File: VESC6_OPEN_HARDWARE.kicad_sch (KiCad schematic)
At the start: 20 parts, among them P1 USB_OTG, P2 CAN2, P3 SWD, P4 HALL/Encoder, P5 CAN1, P6 ADC_SWITCH

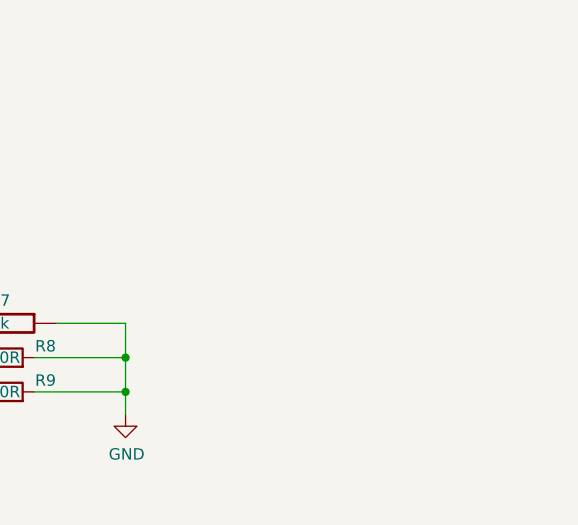
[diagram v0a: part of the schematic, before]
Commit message: mounting holes, more grounding and routing
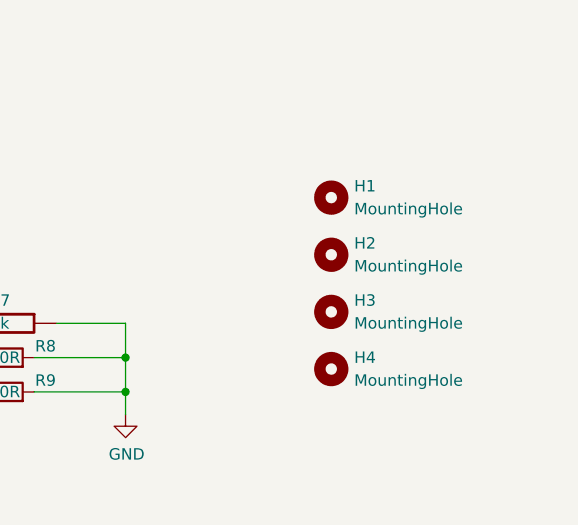
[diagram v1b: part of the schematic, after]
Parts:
- added H1, H2, H3, H4: MountingHole, CustomFootprints:MountingHole_3mm, symbol Mechanical:MountingHole

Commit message: Release
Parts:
- removed D1: BLUE, Diode_SMD:D_0603_1608Metric, symbol Device:LED
- removed R7: 1k, Resistor_SMD:R_0603_1608Metric, symbol BLDC_4-rescue:R-RESCUE-BLDC_4
- D3: value GREEN -> WHITE; LCSC part no. C12624 -> C2290
- P3: LCSC part no. 23390339 -> C160405

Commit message: Release1
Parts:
- D3: Link https://jlcpcb.com/partdetail/EverlightElec-19_217_GHC_YR1S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 -> (none); MFP 19-217/GHC-YR1S2/3T -> (none)
- P1: Link https://jlcpcb.com/partdetail/Korean_HropartsElec-U_D_M5DD_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 -> (none); MFP U-D-M5DD-W-1 -> (none)
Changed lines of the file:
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@@
 			)
 		)
-		(property "Datasheet" "https://www.molex.com/content/dam/molex/molex-dot-com/products/automated/en-us/salesdrawingpdf/505/505567/5055670471_sd.pdf?inline"
+		(property "Datasheet" ""
 			(at 53.34 59.69 0)
 			(effects
@@
 			)
 		)
-		(property "Datasheet" "https://datasheet.lcsc.com/lcsc/1811101510_Everlight-Elec-19-217-GHC-YR1S2-3T_C72043.pdf"
+		(property "Datasheet" ""
 			(at 165.1 153.67 0)
 			(effects
@@
 			)
 		)
-		(property "Link" "https://jlcpcb.com/partdetail/EverlightElec-19_217_GHC_YR1S23T/C72043"
+		(property "Link" ""
 			(at 165.1 153.67 0)
 			(effects
@@
 			)
 		)
-		(property "MFP" "19-217/GHC-YR1S2/3T"
+		(property "MFP" ""
 			(at 165.1 153.67 0)
 			(effects
@@
 			)
 		)
-		(property "Datasheet" "https://www.molex.com/content/dam/molex/molex-dot-com/products/automated/en-us/salesdrawingpdf/482/48258/482580001_sd.pdf?"
+		(property "Datasheet" ""
 			(at 58.42 38.1 0)
 			(effects
@@
 			)
 		)
-		(property "Link" "https://jlcpcb.com/partdetail/Korean_HropartsElec-U_D_M5DD_W1/C145795"
+		(property "Link" ""
 			(at 54.61 36.83 0)
 			(effects
@@
 			)
 		)
-		(property "MFP" "U-D-M5DD-W-1"
+		(property "MFP" ""
 			(at 54.61 36.83 0)
 			(effects
@@
 			)
 		)
-		(property "Datasheet" "~"
+		(property "Datasheet" ""
 			(at 74.93 31.75 0)
 			(effects
@@
 			)
 		)
-		(property "Datasheet" "https://www.molex.com/content/dam/molex/molex-dot-com/products/automated/en-us/salesdrawingpdf/505/505567/5055670471_sd.pdf?inline"
+		(property "Datasheet" ""
 			(at 41.91 59.69 0)
 			(effects
@@
 			)
 		)
-		(property "Datasheet" "~"
+		(property "Datasheet" ""
 			(at 217.17 132.08 0)
 			(effects
@@
 			)
 		)
-		(property "Datasheet" "https://www.molex.com/content/dam/molex/molex-dot-com/products/automated/en-us/salesdrawingpdf/505/505567/5055670671_sd.pdf?inline"
+		(property "Datasheet" ""
 			(at 52.07 91.44 0)
 			(effects
@@
 			)
 		)
-		(property "Datasheet" "https://www.molex.com/content/dam/molex/molex-dot-com/products/automated/en-us/salesdrawingpdf/505/505567/5055670471_sd.pdf?inline"
+		(property "Datasheet" ""
 			(at 102.87 20.32 0)
 			(effects
@@
 			)
 		)
-		(property "Datasheet" "~"
+		(property "Datasheet" ""
 			(at 217.17 138.43 0)
 			(effects
@@
 			)
 		)
-		(property "Datasheet" "https://www.molex.com/content/dam/molex/molex-dot-com/products/automated/en-us/salesdrawingpdf/505/505567/5055670671_sd.pdf?inline"
+		(property "Datasheet" ""
 			(at 54.61 153.67 0)
 			(effects
@@
 			)
 		)
-		(property "Datasheet" "~"
+		(property "Datasheet" ""
 			(at 217.17 151.13 0)
 			(effects
@@
 			)
 		)
-		(property "Datasheet" "~"
+		(property "Datasheet" ""
 			(at 217.17 144.78 0)
 			(effects
